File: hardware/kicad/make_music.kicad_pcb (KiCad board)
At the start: 2 copper layers, 330 x 120 mm, 2 parts, among them J1 LEFT / Pico 1-20, J2 RIGHT / Pico 21-40

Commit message: Route protected Pico music carrier and prepare held review files (#20)
* Place carrier components and define module cable assembly

* Route protected carrier and integrate module fixture mounts

* Prepare checked review exports and exact assembly handoff

* Apply final mechanical review and refresh held outputs

---------

Co-authored-by: John O’Dell <johnodell@Johns-MacBook-Pro.local>
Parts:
- added C1: 100n, MakeMusicCarrier:KEMET_C0603_1608_LevelB, F.Cu at (96.5, 95.0)
- added C10: 100n, MakeMusicCarrier:KEMET_C0603_1608_LevelB, F.Cu at (50.5, 95.0)
- added C11: 100n, MakeMusicCarrier:KEMET_C0603_1608_LevelB, F.Cu at (87.5, 69.0)
- added C12: 100n, MakeMusicCarrier:KEMET_C0603_1608_LevelB, F.Cu at (125.5, 69.0)
- added C13: 4u7 / 25V, Capacitor_SMD:C_0805_2012Metric, F.Cu at (238.8, 71.5)
- added C14: 4u7 / 25V, Capacitor_SMD:C_0805_2012Metric, F.Cu at (241.2, 80.5)
- added C15: 10n / 50V, Capacitor_SMD:C_0603_1608Metric, F.Cu at (247.0, 78.0)
- added C16: 4u7 / 25V, Capacitor_SMD:C_0805_2012Metric, F.Cu at (239.0, 87.0)
- added C2: 100n, MakeMusicCarrier:KEMET_C0603_1608_LevelB, F.Cu at (130.5, 95.0)
- added C3: 100n, MakeMusicCarrier:KEMET_C0603_1608_LevelB, F.Cu at (164.5, 95.0)
- added C4: 100n, MakeMusicCarrier:KEMET_C0603_1608_LevelB, F.Cu at (198.5, 95.0)
- added C5: 100n, MakeMusicCarrier:KEMET_C0603_1608_LevelB, F.Cu at (232.5, 95.0)
- added C6: 100n, MakeMusicCarrier:KEMET_C0603_1608_LevelB, F.Cu at (266.5, 95.0)
- added C7: 100n, MakeMusicCarrier:KEMET_C0603_1608_LevelB, F.Cu at (300.5, 95.0)
- added C8: 100n, MakeMusicCarrier:KEMET_C0603_1608_LevelB, F.Cu at (334.5, 95.0)
- added C9: 100n, MakeMusicCarrier:KEMET_C0603_1608_LevelB, F.Cu at (50.5, 55.0)
- added D2: SS14-E3/61T, MakeMusicCarrier:Vishay_SS14_SMA_K1_A2, F.Cu at (246.0, 83.5)
- added D3: SMAJ5.0CA, MakeMusicPower:Littelfuse_SMAJ5-0CA_DO-214AC, F.Cu at (248.0, 71.5)
- added F1: 1.25A T, MakeMusicPower:Schurter_UMT-H_3403-0275-23, F.Cu at (250.0, 50.0)
- added H1: JST PH battery, Connector_JST:JST_PH_B2B-PH-K_1x02_P2.00mm_Vertical, B.Cu at (249.0, 40.0)
- added J10: C5 / GP26, MakeMusicCarrier:Harwin_M20-9990346_1x3_P2.54mm, F.Cu at (325.5, 95.0)
- added J11: Semitone up / GP27, MakeMusicCarrier:Harwin_M20-9990346_1x3_P2.54mm, F.Cu at (41.5, 55.0)
- added J12: Octave up / GP28, MakeMusicCarrier:Harwin_M20-9990346_1x3_P2.54mm, F.Cu at (41.5, 95.0)
- added J13: Buzzer 1 / PWM / GP13, MakeMusicCarrier:Harwin_M20-9990346_1x3_P2.54mm, F.Cu at (78.5, 69.0)
- added J14: Buzzer 2 / PWM / GP12, MakeMusicCarrier:Harwin_M20-9990346_1x3_P2.54mm, F.Cu at (116.5, 69.0)
- added J15: GPIO / Harwin 16-way, MakeMusicCarrier:Harwin_M20-9991646_1x16_P2.54mm, F.Cu at (70.0, 32.0)
- added J3: C4 / GP16, MakeMusicCarrier:Harwin_M20-9990346_1x3_P2.54mm, F.Cu at (87.5, 95.0)
- added J4: D4 / GP17, MakeMusicCarrier:Harwin_M20-9990346_1x3_P2.54mm, F.Cu at (121.5, 95.0)
- added J5: E4 / GP18, MakeMusicCarrier:Harwin_M20-9990346_1x3_P2.54mm, F.Cu at (155.5, 95.0)
- added J6: F4 / GP19, MakeMusicCarrier:Harwin_M20-9990346_1x3_P2.54mm, F.Cu at (189.5, 95.0)
- added J7: G4 / GP20, MakeMusicCarrier:Harwin_M20-9990346_1x3_P2.54mm, F.Cu at (223.5, 95.0)
- added J8: A4 / GP21, MakeMusicCarrier:Harwin_M20-9990346_1x3_P2.54mm, F.Cu at (257.5, 95.0)
- added J9: B4 / GP22, MakeMusicCarrier:Harwin_M20-9990346_1x3_P2.54mm, F.Cu at (291.5, 95.0)
- added MH1: MountingHole_3.2mm_M3, MountingHole_3.2mm_M3, F.Cu at (26.0, 26.0)
- added MH10: MountingHole_3.2mm_M3, MountingHole_3.2mm_M3, F.Cu at (65.0, 103.0)
- added MH11: MountingHole_3.2mm_M3, MountingHole_3.2mm_M3, F.Cu at (70.0, 134.0)
- added MH12: MountingHole_3.2mm_M3, MountingHole_3.2mm_M3, F.Cu at (175.0, 134.0)
- added MH13: MountingHole_3.2mm_M3, MountingHole_3.2mm_M3, F.Cu at (277.0, 134.0)
- added MH14: MountingHole_3.2mm_M3, MountingHole_3.2mm_M3, F.Cu at (311.0, 134.0)
- added MH15: MountingHole_3.2mm_M3, MountingHole_3.2mm_M3, F.Cu at (175.0, 93.0)
- added MH16: MountingHole_3.2mm_M3, MountingHole_3.2mm_M3, F.Cu at (209.0, 93.0)
- added MH17: MountingHole_3.2mm_M3, MountingHole_3.2mm_M3, F.Cu at (311.0, 93.0)
- added MH2: MountingHole_3.2mm_M3, MountingHole_3.2mm_M3, F.Cu at (344.0, 26.0)
- added MH3: MountingHole_3.2mm_M3, MountingHole_3.2mm_M3, F.Cu at (26.0, 134.0)
- added MH4: MountingHole_3.2mm_M3, MountingHole_3.2mm_M3, F.Cu at (344.0, 134.0)
- added MH5: MountingHole_3.2mm_M3, MountingHole_3.2mm_M3, F.Cu at (170.0, 37.0)
- added MH6: MountingHole_3.2mm_M3, MountingHole_3.2mm_M3, F.Cu at (230.0, 37.0)
- added MH7: MountingHole_3.2mm_M3, MountingHole_3.2mm_M3, F.Cu at (170.0, 63.0)
- added MH8: MountingHole_3.2mm_M3, MountingHole_3.2mm_M3, F.Cu at (230.0, 63.0)
- added MH9: MountingHole_3.2mm_M3, MountingHole_3.2mm_M3, F.Cu at (28.0, 94.0)
- added R1: 10k, Resistor_SMD:R_0603_1608Metric, F.Cu at (79.0, 63.0)
- added R2: 10k, Resistor_SMD:R_0603_1608Metric, F.Cu at (117.0, 63.0)
- added R3: 649k, Resistor_SMD:R_0603_1608Metric, F.Cu at (235.0, 73.0)
- added R4: 332k, Resistor_SMD:R_0603_1608Metric, F.Cu at (235.0, 75.0)
- added R5: 1.05M, Resistor_SMD:R_0603_1608Metric, F.Cu at (235.0, 78.5)
- added R6: 332k, Resistor_SMD:R_0603_1608Metric, F.Cu at (235.0, 80.5)
- added R7: 3.32k, Resistor_SMD:R_0603_1608Metric, F.Cu at (244.0, 74.3)
- added R8: 100, Resistor_SMD:R_0603_1608Metric, F.Cu at (244.0, 78.0)
- added S1: MN12SS1W03, MakeMusicCarrier:NKK_MN12SS1W03_TerminalPattern_Candidate, F.Cu at (270.0, 75.0)
- added TP1: USB VBUS only, TestPoint:TestPoint_Pad_D2.0mm, F.Cu at (157.0, 23.0)
- added U2: TPS259474LRPWR, MakeMusicPower:TI_RPW0010A_TPS259474_2x2mm, F.Cu at (240.0, 76.0)
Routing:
- net /GND: track 0.00 -> 639.2 mm, vias 0 -> 24
- net /3V3_OUT: track 0.00 -> 576.1 mm, vias 0 -> 1
- net /GP26: track 0.00 -> 210.2 mm, vias 0 -> 1
- net /GP22: track 0.00 -> 184.2 mm, vias 0 -> 1
- net /GP21: track 0.00 -> 155.4 mm, vias 0 -> 1
- net /GP28: track 0.00 -> 135.0 mm
- net /VSYS: track 0.00 -> 131.5 mm, vias 0 -> 1
- net /GP27: track 0.00 -> 125.7 mm, vias 0 -> 1
- net /GP20: track 0.00 -> 90.4 mm, vias 0 -> 1
- net /GP16: track 0.00 -> 79.9 mm
- net /Battery protection/BAT_SW_PLUS: track 0.00 -> 68.4 mm
- net /GP15: track 0.00 -> 67.0 mm
- net /GP14: track 0.00 -> 67.0 mm
- net /GP13: track 0.00 -> 66.8 mm
- net /GP1: track 0.00 -> 65.5 mm
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- added copper zone on B.Cu, net /GND
- added copper zone on F.Cu, net /GND
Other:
- board text added: "1 +"
- board text added: "1:S 2:3V3 3:G"
- board text added: "2 GND"
- board text added: "330 x 120; module body outlines are references; separate mounting fixture required"
- board text added: "3V3"
- board text added: "BATTERY OFF"
- board text added: "EXPANSION 3.3V ONLY"
- board text added: "GND"
- board text added: "GP0"
- board text added: "GP1"
- board text added: "GP10"
- board text added: "GP11"
- board text added: "GP14"
- board text added: "GP15"
- board text added: "GP2"
- board text added: "GP3"
- board text added: "GP4"
- board text added: "GP5"
- board text added: "GP6"
- board text added: "GP7"
- board text added: "GP8"
- board text added: "GP9"
- board text added: "MAKE MUSIC - CARRIER P1"
- board text added: "OCTAVE"
- board text added: "OCTAVE +"
- board text added: "ON"
- board text added: "P1 CARRIER LAYOUT REVIEW - PHYSICAL FIT PENDING"
- board text added: "PICO - REMOVE POWER TO UNPLUG"
- board text added: "POWER CIRCUIT"
- board text added: "PROTECTED 1S / EXTERNAL CHARGE"
- board text added: "PROTOTYPE / FIT VALIDATION REQUIRED"
- board text added: "REMOVABLE PICO"
- board text added: "SEMITONE"
- board text added: "SEMITONE +"
- board text added: "ST0238 1"
- board text added: "ST0238 2"
- board text added: "TOUCH A4"
- board text added: "TOUCH B4"
- board text added: "TOUCH C4"
- board text added: "TOUCH C5"
- board text added: "TOUCH D4"
- board text added: "TOUCH E4"
- board text added: "TOUCH F4"
- board text added: "TOUCH G4"
- board text added: "UNDERSIDE INSULATING CASSETTE"
- board text removed: "330 x 120 mm proposed; paper fit and remaining parts pending"
- board text removed: "Body rectangles are reference drawings, not component footprints or mounting holes."
- board text removed: "GPIO HEADER - TBD"
- board text removed: "OCTAVE+"
- board text removed: "PICO USB END"
- board text removed: "PLACEMENT DRAFT - UNROUTED - NOT FOR FABRICATION"
- board text removed: "POWER PARTS - TBD"
- board text removed: "SEMITONE+"
- board text removed: "ST0238"
- board text removed: "UNDERSIDE BATTERY - MOUNT TBD"

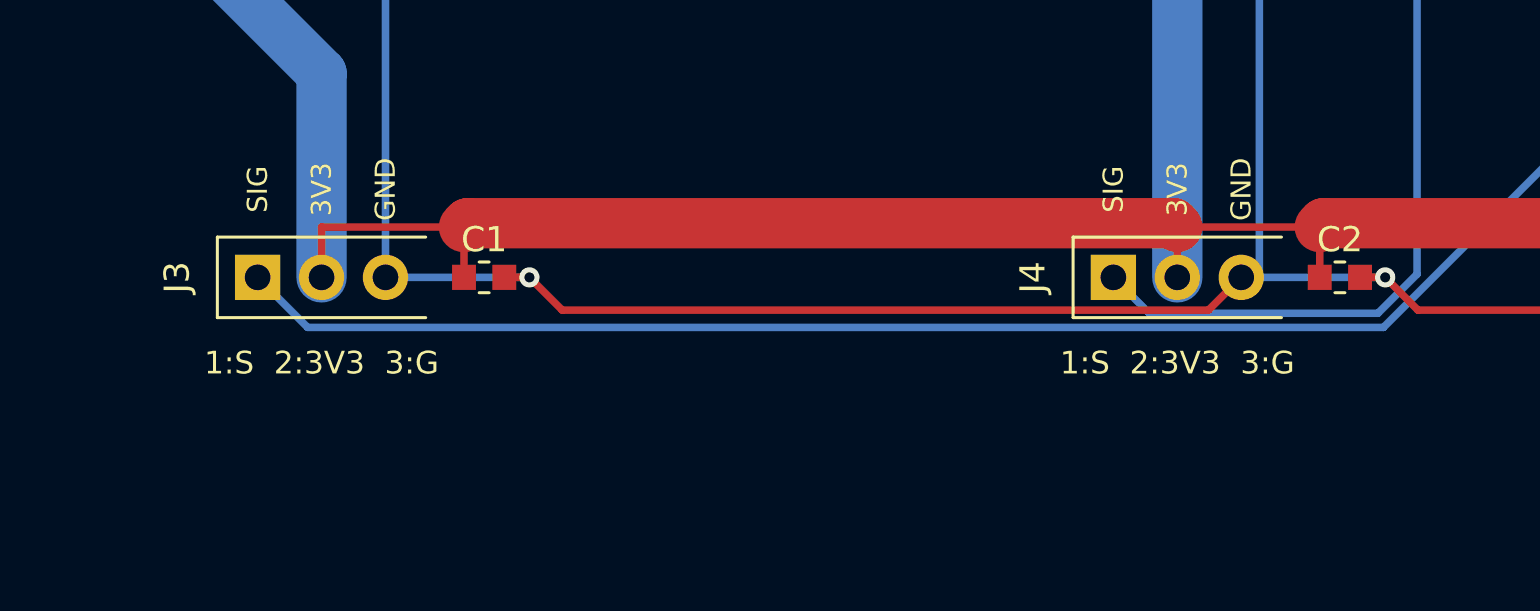
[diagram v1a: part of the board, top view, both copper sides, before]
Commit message: Correct note connector clearance and preserve PCB build checkpoint
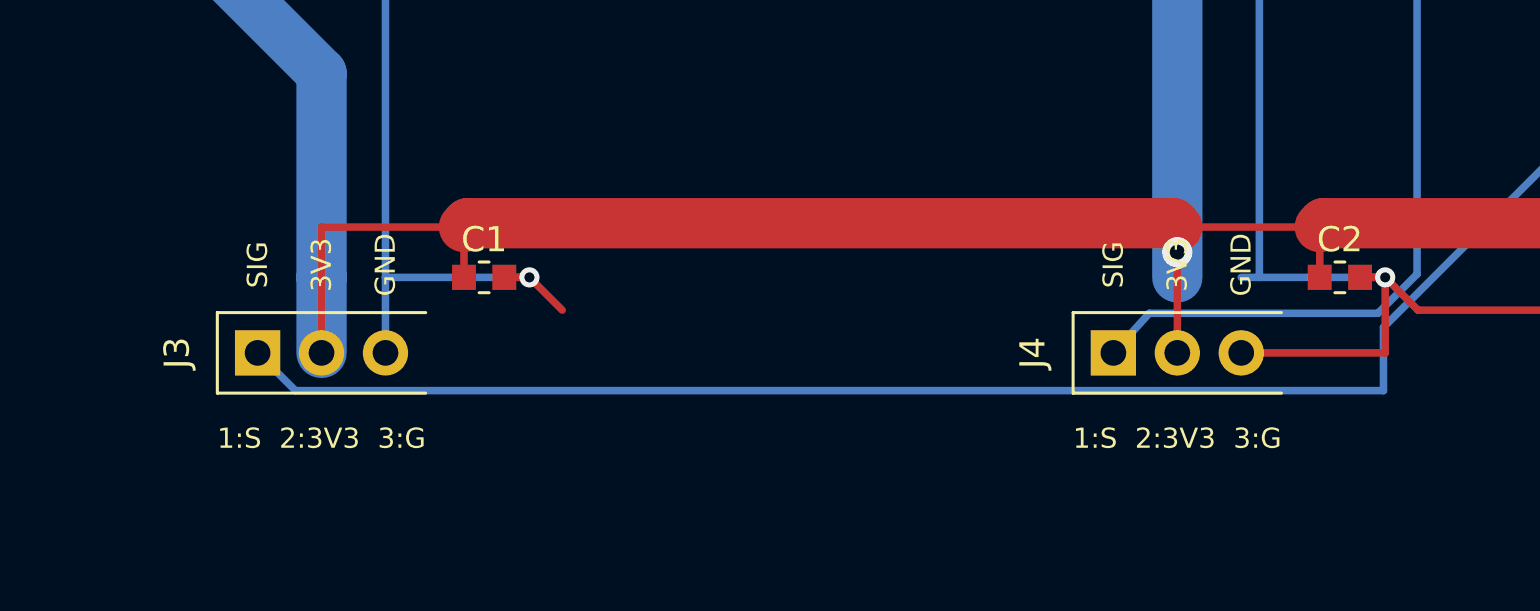
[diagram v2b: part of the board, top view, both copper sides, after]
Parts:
- moved J3 3.00 mm to (87.5, 98.0)
- moved J4 3.00 mm to (121.5, 98.0)
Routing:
- net /GND: track 639.2 -> 623.4 mm
- net /3V3_OUT: track 576.1 -> 585.1 mm, vias 1 -> 2
- net /GP16: track 79.9 -> 82.2 mm
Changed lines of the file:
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@@
 	(footprint "MakeMusicCarrier:Harwin_M20-9990346_1x3_P2.54mm"
 		(layer "F.Cu")
-		(at 121.46 95 90)
+		(at 121.46 98 90)
 		(descr "Carrier cable/expansion header candidate; Harwin M20-999 drawing issue23: 2.54 pitch,1.02 holes; carrier-defined numbering. See carrier-interfaces.md")
 		(property "Reference" "J4"
@@
 	(footprint "MakeMusicCarrier:Harwin_M20-9990346_1x3_P2.54mm"
 		(layer "F.Cu")
-		(at 87.46 95 90)
+		(at 87.46 98 90)
 		(descr "Carrier cable/expansion header candidate; Harwin M20-999 drawing issue23: 2.54 pitch,1.02 holes; carrier-defined numbering. See carrier-interfaces.md")
 		(property "Reference" "J3"
@@
 	)
 	(gr_text "1:S  2:3V3  3:G"
+		(at 90 101.4 0)
+		(layer "F.SilkS")
+		(effects
+			(font
+				(size 0.8 0.8)
+				(thickness 0.12)
+			)
+		)
+	)
+	(gr_text "1:S  2:3V3  3:G"
+		(at 124 101.4 0)
+		(layer "F.SilkS")
+		(effects
+			(font
+				(size 0.8 0.8)
+				(thickness 0.12)
+			)
+		)
+	)
+	(gr_text "1:S  2:3V3  3:G"
 		(at 44 58.4 0)
 		(layer "F.SilkS")
@@
 	)
 	(gr_text "1:S  2:3V3  3:G"
-		(at 90 98.4 0)
-		(layer "F.SilkS")
-		(effects
-			(font
-				(size 0.9 0.9)
-				(thickness 0.15)
-			)
-		)
-	)
-	(gr_text "1:S  2:3V3  3:G"
 		(at 119 72.4 0)
 		(layer "F.SilkS")
@@
 	)
 	(gr_text "1:S  2:3V3  3:G"
-		(at 124 98.4 0)
-		(layer "F.SilkS")
-		(effects
-			(font
-				(size 0.9 0.9)
-				(thickness 0.15)
-			)
-		)
-	)
-	(gr_text "1:S  2:3V3  3:G"
 		(at 157.999999 98.4 0)
 		(layer "F.SilkS")
@@
 	)
 	(segment
-		(start 125.2383 96.3017)
-		(end 126.54 95)
-		(width 0.3)
-		(layer "F.Cu")
-		(net "/GND")
-	)
-	(segment
 		(start 202.7063 97.4463)
 		(end 200.26 95)
@@
 	)
 	(segment
+		(start 126.54 98)
+		(end 132.259999 98)
+		(width 0.3)
+		(layer "F.Cu")
+		(net "/GND")
+	)
+	(segment
 		(start 267.259999 95)
 		(end 268.259999 95)
@@
 	)
 	(segment
-		(start 88.26 69)
-		(end 89.26 69)
+		(start 132.259999 98)
+		(end 132.259999 95)
 		(width 0.3)
-		(locked yes)
 		(layer "F.Cu")
 		(net "/GND")
 	)
 	(segment
-		(start 242.15 80.5)
-		(end 243.2 80.5)
+		(start 88.26 69)
+		(end 89.26 69)
 		(width 0.3)
 		(locked yes)
@@
 	)
 	(segment
-		(start 99.5617 96.3017)
-		(end 125.2383 96.3017)
+		(start 242.15 80.5)
+		(end 243.2 80.5)
 		(width 0.3)
+		(locked yes)
 		(layer "F.Cu")
 		(net "/GND")
@@
 	)
 	(segment
+		(start 92.54 95)
+		(end 92.54 98)
+		(width 0.3)
+		(layer "B.Cu")
+		(net "/GND")
+	)
+	(segment
 		(start 268.26 95)
 		(end 262.54 95)
@@
 	)
 	(segment
+		(start 124 95)
+		(end 124 98)
+		(width 0.3)
+		(layer "F.Cu")
+		(net "/3V3_OUT")
+	)
+	(segment
 		(start 44 95)
 		(end 44 93)
@@
 	)
 	(segment
+		(start 90 95)
+		(end 90 98)
+		(width 0.3)
+		(layer "F.Cu")
+		(net "/3V3_OUT")
+	)
+	(segment
 		(start 157.999999 93)
 		(end 163.659999 93)
@@
 		(net "/3V3_OUT")
 	)
+	(via
+		(at 124 94)
+		(size 1.2)
+		(drill 0.6)
+		(layers "F.Cu" "B.Cu")
+		(net "/3V3_OUT")
+	)
 	(segment
 		(start 67.2488 69.075)
@@
 	)
 	(segment
+		(start 90 95)
+		(end 90 98)
+		(width 2)
+		(layer "B.Cu")
+		(net "/3V3_OUT")
+	)
+	(segment
 		(start 189.765 98.2685)
 		(end 160.7412 98.2685)
@@
 	)
 	(segment
-		(start 133.5255 94.8734)
-		(end 131.9722 96.4267)
+		(start 122.8867 96.4267)
+		(end 121.46 98)
 		(width 0.3)
 		(layer "B.Cu")
@@
 	)
 	(segment
-		(start 131.9722 96.4267)
-		(end 122.8867 96.4267)
+		(start 133.5255 94.8734)
+		(end 131.9722 96.4267)
 		(width 0.3)
 		(layer "B.Cu")
@@
 	)
 	(segment
-		(start 122.8867 96.4267)
-		(end 121.46 95)
+		(start 131.9722 96.4267)
+		(end 122.8867 96.4267)
 		(width 0.3)
 		(layer "B.Cu")
@@
 	)
 	(segment
-		(start 89.4483 96.9883)
-		(end 87.46 95)
+		(start 132.1908 96.9883)
+		(end 132.1908 99.5)
 		(width 0.3)
 		(layer "B.Cu")
@@
 	)
 	(segment
-		(start 132.1908 96.9883)
-		(end 89.4483 96.9883)
+		(start 132.1908 99.5)
+		(end 88.96 99.5)
 		(width 0.3)
 		(layer "B.Cu")
@@
 		(width 0.3)
 		(layer "B.Cu")
+		(net "/GP16")
+	)
+	(segment
+		(start 88.96 99.5)
+		(end 87.46 98)
+		(width 0.3)
+		(layer "B.Cu")

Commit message: Move battery interface for 18650 and define five complete assemblies
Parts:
- moved H1 40.0 mm to (289.0, 40.0)
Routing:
- net /Battery protection/BAT_PROT_PLUS: track 26.1 -> 66.3 mm
- net /GND: track 623.4 -> 589.9 mm
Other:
- board text added: "18650 CASSETTE - FIT REVIEW"
- board text added: "BH-18650-W MAX BODY / BELOW"
- board text added: "PARTIAL B.Cu RESTRICTION"
- board text removed: "UNDERSIDE INSULATING CASSETTE"
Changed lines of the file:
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@@
 	(footprint "Connector_JST:JST_PH_B2B-PH-K_1x02_P2.00mm_Vertical"
 		(layer "B.Cu")
-		(at 249 40)
+		(at 289 40)
 		(descr "JST PH series connector, B2B-PH-K (http://www.jst-mfg.com/product/pdf/eng/ePH.pdf)")
 		(tags "connector JST PH vertical")
@@
 		)
 	)
+	(gr_poly
+		(pts
+			(xy 165 32) (xy 165.12 32) (xy 165.12 68) (xy 165 68)
+		)
+		(stroke
+			(width 0)
+			(type default)
+		)
+		(fill yes)
+		(layer "Dwgs.User")
+	)
+	(gr_poly
+		(pts
+			(xy 165 32) (xy 277 32) (xy 277 32.119999) (xy 165 32.119999)
+		)
+		(stroke
+			(width 0)
+			(type default)
+		)
+		(fill yes)
+		(layer "Dwgs.User")
+	)
+	(gr_poly
+		(pts
+			(xy 165 67.88) (xy 277 67.88) (xy 277 67.999999) (xy 165 67.999999)
+		)
+		(stroke
+			(width 0)
+			(type default)
+		)
+		(fill yes)
+		(layer "Dwgs.User")
+	)
+	(gr_poly
+		(pts
+			(xy 181.9 39.3) (xy 182.02 39.3) (xy 182.02 60.7) (xy 181.9 60.7)
+		)
+		(stroke
+			(width 0)
+			(type default)
+		)
+		(fill yes)
+		(layer "Dwgs.User")
+	)
+	(gr_poly
+		(pts
+			(xy 181.9 39.3) (xy 260.1 39.3) (xy 260.1 39.42) (xy 181.9 39.42)
+		)
+		(stroke
+			(width 0)
+			(type default)
+		)
+		(fill yes)
+		(layer "Dwgs.User")
+	)
+	(gr_poly
+		(pts
+			(xy 181.9 60.58) (xy 260.1 60.58) (xy 260.1 60.7) (xy 181.9 60.7)
+		)
+		(stroke
+			(width 0)
+			(type default)
+		)
+		(fill yes)
+		(layer "Dwgs.User")
+	)
+	(gr_poly
+		(pts
+			(xy 259.98 39.3) (xy 260.1 39.3) (xy 260.1 60.7) (xy 259.98 60.7)
+		)
+		(stroke
+			(width 0)
+			(type default)
+		)
+		(fill yes)
+		(layer "Dwgs.User")
+	)
+	(gr_poly
+		(pts
+			(xy 276.88 32) (xy 277 32) (xy 277 68) (xy 276.88 68)
+		)
+		(stroke
+			(width 0)
+			(type default)
+		)
+		(fill yes)
+		(layer "Dwgs.User")
+	)
 	(gr_line
 		(start 32 62)
@@
 		)
 	)
+	(gr_text "PARTIAL B.Cu RESTRICTION"
+		(at 200 66 0)
+		(layer "Dwgs.User")
+		(effects
+			(font
+				(size 0.8 0.8)
+				(thickness 0.12)
+			)
+		)
+	)
+	(gr_text "BH-18650-W MAX BODY / BELOW"
+		(at 221 55 0)
+		(layer "Dwgs.User")
+		(effects
+			(font
+				(size 0.85 0.85)
+				(thickness 0.1275)
+			)
+		)
+	)
+	(gr_text "18650 CASSETTE - FIT REVIEW"
+		(at 221 30 0)
+		(layer "Dwgs.User")
+		(effects
+			(font
+				(size 1 1)
+				(thickness 0.15)
+			)
+		)
+	)
 	(gr_text "SEMITONE"
 		(at 44 74 0)
@@
 		)
 	)
-	(gr_text "UNDERSIDE INSULATING CASSETTE"
-		(at 200 50 0)
-		(layer "Dwgs.User")
-		(effects
-			(font
-				(size 1 1)
-				(thickness 0.15)
-			)
-		)
-	)
 	(gr_text "330 x 120; module body outlines are references; separate mounting fixture required"
 		(at 205 18 0)
@@
 	)
 	(segment
-		(start 251 40)
-		(end 252.0017 40)
-		(width 0.3)
-		(layer "B.Cu")
-		(net "/GND")
-	)
-	(segment
 		(start 127.26 95)
 		(end 127.26 69)
@@
 	)
 	(segment
-		(start 252.0017 40)
-		(end 252.0017 72.4983)
-		(width 0.3)
-		(layer "B.Cu")
-		(net "/GND")
-	)
-	(segment
 		(start 52.8181 95)
 		(end 70 77.8181)
@@
 	)
 	(segment
-		(start 249 40)
-		(end 238 40)
+		(start 289 40)
+		(end 288.5 40.5)
 		(width 1.5)
-		(locked yes)
 		(layer "F.Cu")
 		(net "/Battery protection/BAT_PROT_PLUS")
@@
 		(layer "F.Cu")
 		(net "/Battery protection/BAT_PROT_PLUS")
+	)
+	(segment
+		(start 288.5 40.5)
+		(end 238 40.5)
+		(width 1.5)
+		(layer "F.Cu")
+		(net "/Battery protection/BAT_PROT_PLUS")

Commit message: Route buzzer bulk capacitors and verify live PCB integration
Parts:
- added C17: 10u / 10V, Capacitor_SMD:C_0805_2012Metric, F.Cu at (87.5, 65.5)
- added C18: 10u / 10V, Capacitor_SMD:C_0805_2012Metric, F.Cu at (125.5, 65.5)
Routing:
- net /GND: track 589.9 -> 597.6 mm
- net /3V3_OUT: track 585.1 -> 588.2 mm

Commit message: Clear rear socket markers and verify final 18650 carrier outline
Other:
- board size 330 x 120 mm -> 330 x 121.5 mm
- board text added: "330 x 121.5; service datum (20,20); module outlines are references; fit validation required"
- board text removed: "330 x 120; module body outlines are references; separate mounting fixture required"
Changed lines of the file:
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@@
 	)
 	(gr_line
-		(start 20 20)
-		(end 350 20)
+		(start 20 18.5)
+		(end 350 18.5)
 		(stroke
-			(width 0.1)
+			(width 0.05)
 			(type default)
 		)
@@
 	(gr_line
 		(start 20 140)
-		(end 20 20)
+		(end 20 18.5)
 		(stroke
-			(width 0.1)
+			(width 0.05)
 			(type default)
 		)
@@
 	)
 	(gr_line
-		(start 350 20)
+		(start 350 18.5)
 		(end 350 140)
 		(stroke
-			(width 0.1)
+			(width 0.05)
 			(type default)
 		)
@@
 		(end 20 140)
 		(stroke
-			(width 0.1)
+			(width 0.05)
 			(type default)
 		)
@@
 		)
 	)
+	(gr_text "SEMITONE"
+		(at 44 74 0)
+		(layer "Dwgs.User")
+		(effects
+			(font
+				(size 1 1)
+				(thickness 0.15)
+			)
+		)
+	)
+	(gr_text "OCTAVE"
+		(at 44 114 0)
+		(layer "Dwgs.User")
+		(effects
+			(font
+				(size 1 1)
+				(thickness 0.15)
+			)
+		)
+	)
+	(gr_text "ST0238 1"
+		(at 80 87.5 0)
+		(layer "Dwgs.User")
+		(effects
+			(font
+				(size 1 1)
+				(thickness 0.15)
+			)
+		)
+	)
+	(gr_text "TOUCH C4"
+		(at 90 114 0)
+		(layer "Dwgs.User")
+		(effects
+			(font
+				(size 1 1)
+				(thickness 0.15)
+			)
+		)
+	)
+	(gr_text "ST0238 2"
+		(at 118 87.5 0)
+		(layer "Dwgs.User")
+		(effects
+			(font
+				(size 1 1)
+				(thickness 0.15)
+			)
+		)
+	)
+	(gr_text "TOUCH D4"
+		(at 124 114 0)
+		(layer "Dwgs.User")
+		(effects
+			(font
+				(size 1 1)
+				(thickness 0.15)
+			)
+		)
+	)
+	(gr_text "REMOVABLE PICO"
+		(at 140 45.5 0)
+		(layer "Dwgs.User")
+		(effects
+			(font
+				(size 1 1)
+				(thickness 0.15)
+			)
+		)
+	)
+	(gr_text "TOUCH E4"
+		(at 158 114 0)
+		(layer "Dwgs.User")
+		(effects
+			(font
+				(size 1 1)
+				(thickness 0.15)
+			)
+		)
+	)
+	(gr_text "TOUCH F4"
+		(at 192 114 0)
+		(layer "Dwgs.User")
+		(effects
+			(font
+				(size 1 1)
+				(thickness 0.15)
+			)
+		)
+	)
 	(gr_text "18650 CASSETTE - FIT REVIEW"
 		(at 221 30 0)
@@
 		)
 	)
-	(gr_text "SEMITONE"
-		(at 44 74 0)
-		(layer "Dwgs.User")
-		(effects
-			(font
-				(size 1 1)
-				(thickness 0.15)
-			)
-		)
-	)
-	(gr_text "OCTAVE"
-		(at 44 114 0)
-		(layer "Dwgs.User")
-		(effects
-			(font
-				(size 1 1)
-				(thickness 0.15)
-			)
-		)
-	)
-	(gr_text "ST0238 1"
-		(at 80 87.5 0)
-		(layer "Dwgs.User")
-		(effects
-			(font
-				(size 1 1)
-				(thickness 0.15)
-			)
-		)
-	)
-	(gr_text "TOUCH C4"
-		(at 90 114 0)
-		(layer "Dwgs.User")
-		(effects
-			(font
-				(size 1 1)
-				(thickness 0.15)
-			)
-		)
-	)
-	(gr_text "ST0238 2"
-		(at 118 87.5 0)
-		(layer "Dwgs.User")
-		(effects
-			(font
-				(size 1 1)
-				(thickness 0.15)
-			)
-		)
-	)
-	(gr_text "TOUCH D4"
-		(at 124 114 0)
-		(layer "Dwgs.User")
-		(effects
-			(font
-				(size 1 1)
-				(thickness 0.15)
-			)
-		)
-	)
-	(gr_text "REMOVABLE PICO"
-		(at 140 45.5 0)
-		(layer "Dwgs.User")
-		(effects
-			(font
-				(size 1 1)
-				(thickness 0.15)
-			)
-		)
-	)
-	(gr_text "TOUCH E4"
-		(at 158 114 0)
-		(layer "Dwgs.User")
-		(effects
-			(font
-				(size 1 1)
-				(thickness 0.15)
-			)
-		)
-	)
-	(gr_text "TOUCH F4"
-		(at 192 114 0)
-		(layer "Dwgs.User")
-		(effects
-			(font
-				(size 1 1)
-				(thickness 0.15)
-			)
-		)
-	)
-	(gr_text "330 x 120; module body outlines are references; separate mounting fixture required"
-		(at 205 18 0)
-		(layer "Dwgs.User")
-		(effects
-			(font
-				(size 1 1)
-				(thickness 0.15)
-			)
-		)
-	)
 	(gr_text "TOUCH G4"
 		(at 226 114 0)
@@
 			)
 		)
+	)
+	(gr_text "330 x 121.5; service datum (20,20); module outlines are references; fit validation required"
+		(at 205 17 0)
+		(layer "Dwgs.User")
+		(effects
+			(font
+				(size 1.1 1.1)
+				(thickness 0.165)
+			)
+		)
